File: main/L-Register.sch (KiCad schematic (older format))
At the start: 19 parts, among them U86 74LS245, U87 74LS173, U88 74LS173

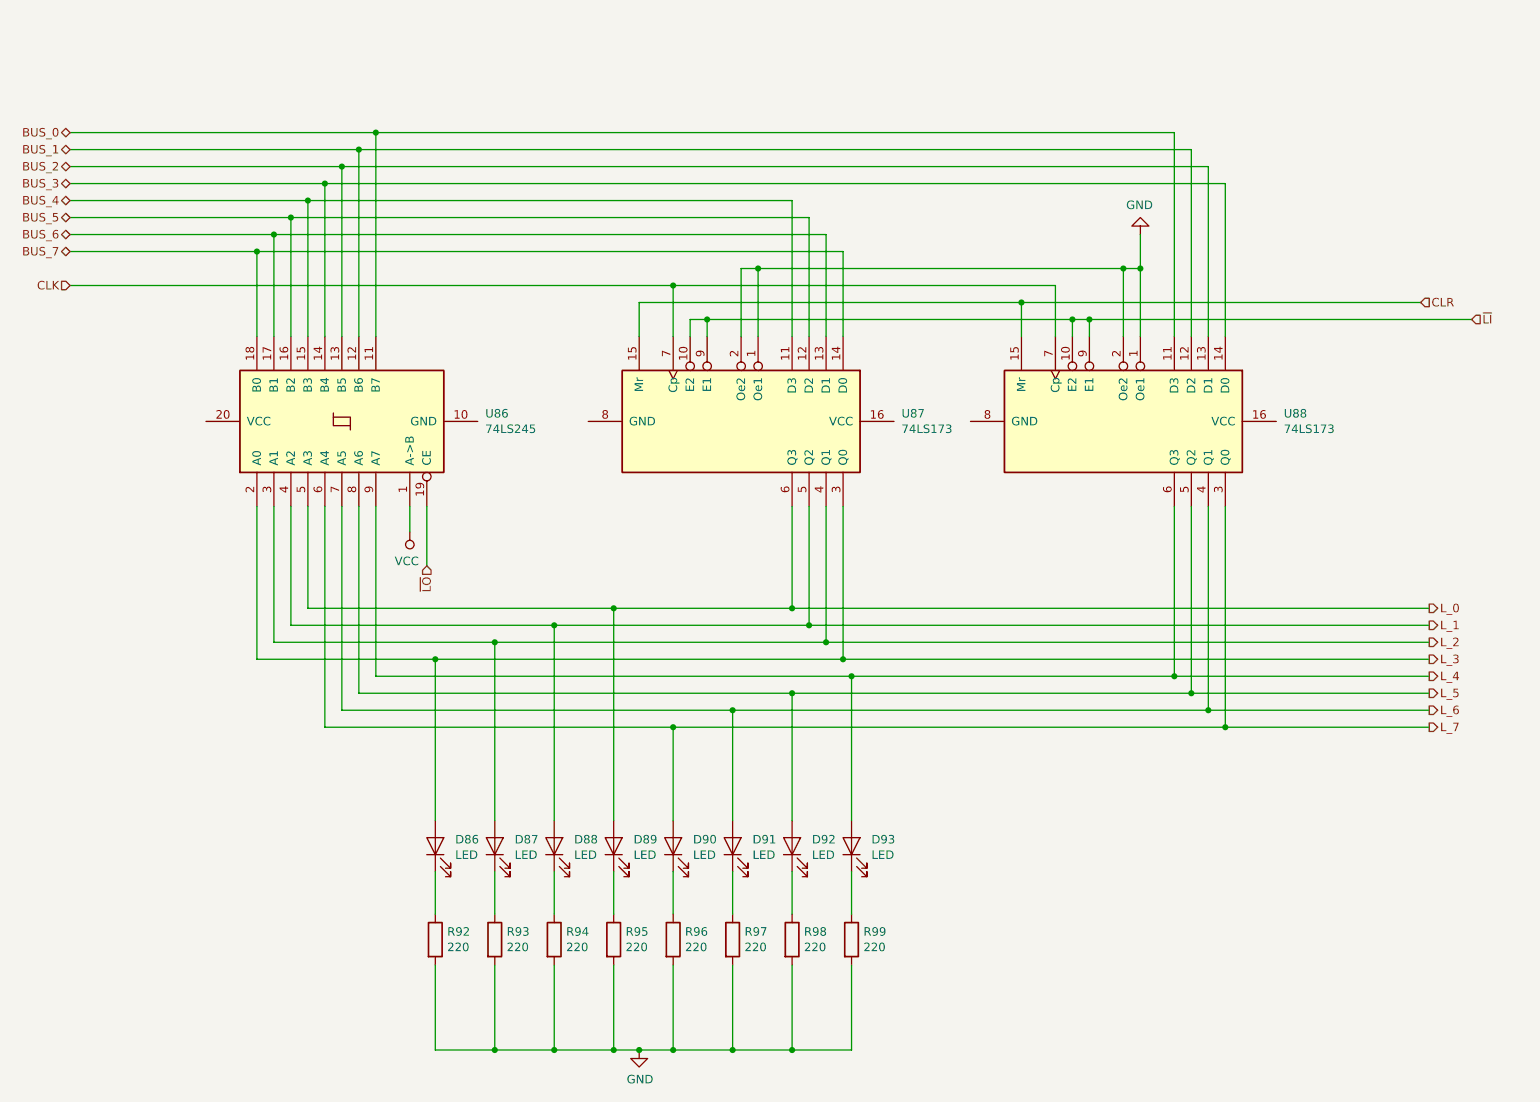
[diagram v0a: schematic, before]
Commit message: Replot main with symbols
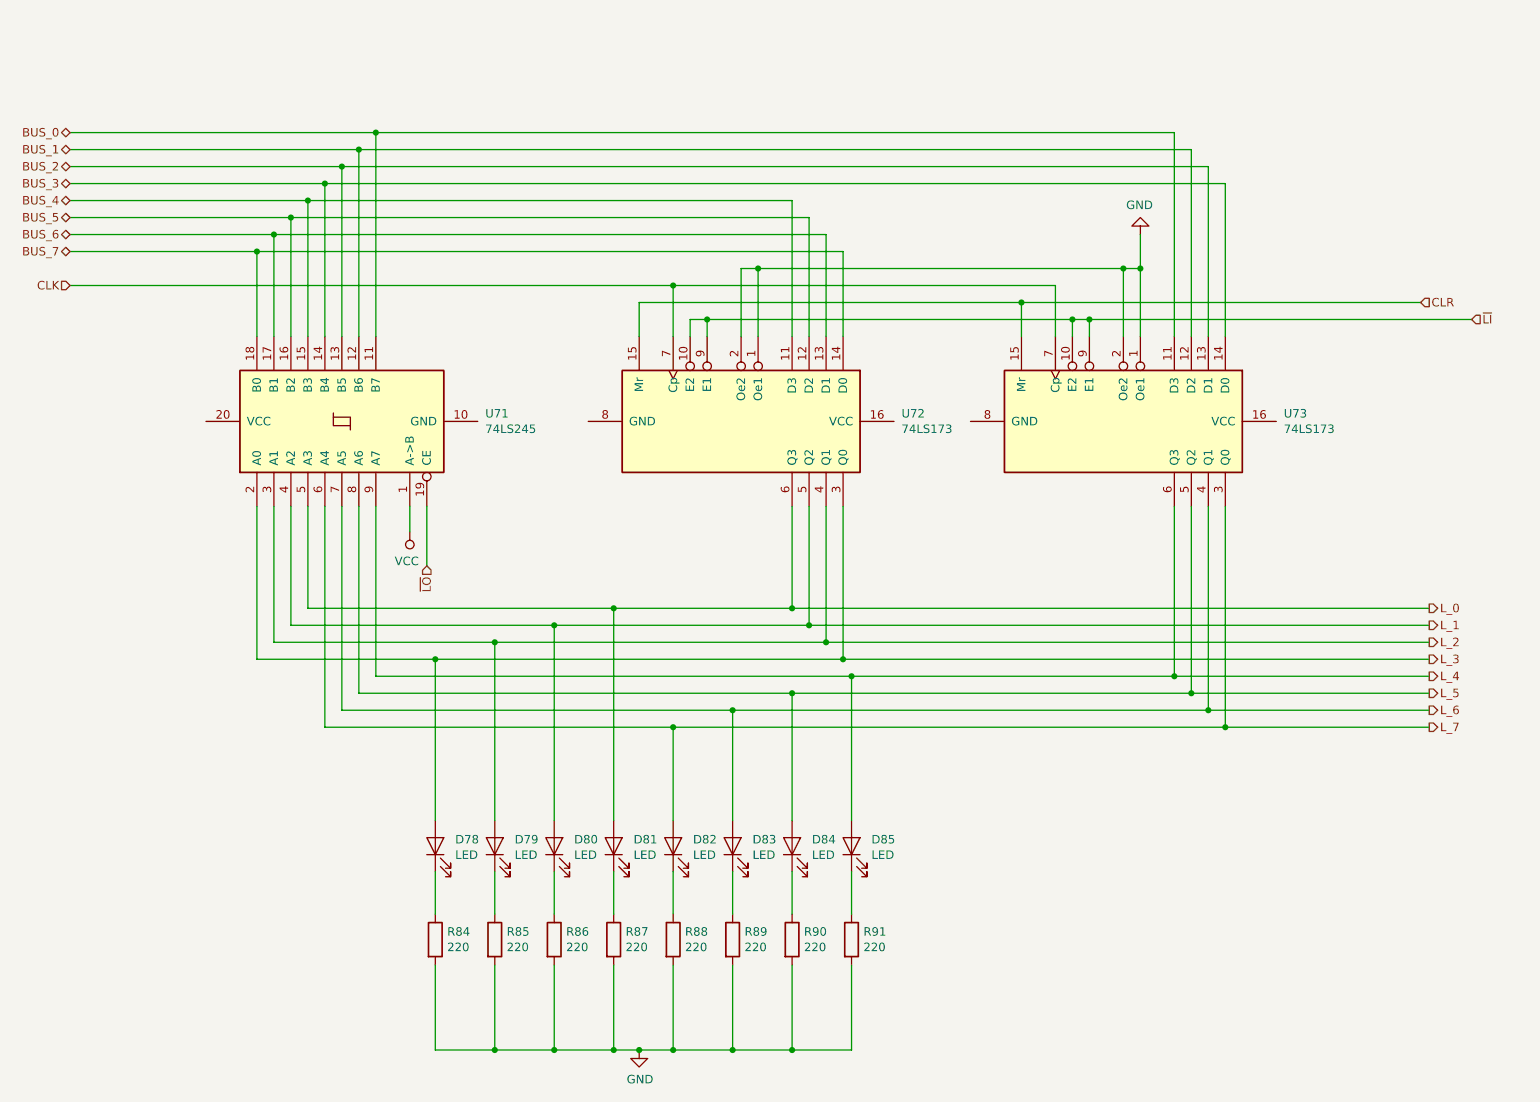
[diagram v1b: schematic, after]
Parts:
- renumbered D86 to D78, D87 to D79, D88 to D80, D89 to D81, D90 to D82, D91 to D83, D92 to D84, D93 to D85, R92 to R84, R93 to R85, R94 to R86, R95 to R87, R96 to R88, R97 to R89, R98 to R90, R99 to R91, U86 to U71, U87 to U72, U88 to U73
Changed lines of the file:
@@
 Sheet 20 26
 Title "L Register"
-Date "2019-11-13"
+Date "2019-11-17"
 Rev "v1.0"
 Comp "Christopher Milan"
@@
 AR Path="/5D9C73BD/5DA803F5" Ref="U?"  Part="1"
 AR Path="/5D9E8F35/5DA803F5" Ref="U?"  Part="1"
-AR Path="/5DA98D6D/5DA9A5C9/5DA803F5" Ref="U86"  Part="1"
-F 0 "U86" V 2896 2456 50  0000 R CNN
+AR Path="/5DA98D6D/5DA9A5C9/5DA803F5" Ref="U71"  Part="1"
+F 0 "U71" V 2896 2456 50  0000 R CNN
 F 1 "74LS245" V 2805 2456 50  0000 R CNN
 F 2 "" H 2850 3300 50  0001 C CNN
@@
 AR Path="/5D9C73BD/5DA80422" Ref="U?"  Part="1"
 AR Path="/5D9E8F35/5DA80422" Ref="U?"  Part="1"
-AR Path="/5DA98D6D/5DA9A5C9/5DA80422" Ref="U88"  Part="1"
-F 0 "U88" V 7404 4244 50  0000 L CNN
+AR Path="/5DA98D6D/5DA9A5C9/5DA80422" Ref="U73"  Part="1"
+F 0 "U73" V 7404 4244 50  0000 L CNN
 F 1 "74LS173" V 7495 4244 50  0000 L CNN
 F 2 "" H 7450 3300 50  0001 C CNN
@@
 AR Path="/5D9C73BD/5DA8044C" Ref="D?"  Part="1"
 AR Path="/5D9E8F35/5DA8044C" Ref="D?"  Part="1"
-AR Path="/5DA98D6D/5DA9A5C9/5DA8044C" Ref="D86"  Part="1"
-F 0 "D86" V 3439 5683 50  0000 R CNN
+AR Path="/5DA98D6D/5DA9A5C9/5DA8044C" Ref="D78"  Part="1"
+F 0 "D78" V 3439 5683 50  0000 R CNN
 F 1 "LED" V 3348 5683 50  0000 R CNN
 F 2 "" H 3400 5800 50  0001 C CNN
@@
 AR Path="/5D9C73BD/5DA80452" Ref="D?"  Part="1"
 AR Path="/5D9E8F35/5DA80452" Ref="D?"  Part="1"
-AR Path="/5DA98D6D/5DA9A5C9/5DA80452" Ref="D87"  Part="1"
-F 0 "D87" V 3789 5683 50  0000 R CNN
+AR Path="/5DA98D6D/5DA9A5C9/5DA80452" Ref="D79"  Part="1"
+F 0 "D79" V 3789 5683 50  0000 R CNN
 F 1 "LED" V 3698 5683 50  0000 R CNN
 F 2 "" H 3750 5800 50  0001 C CNN
@@
 AR Path="/5D9C73BD/5DA80458" Ref="D?"  Part="1"
 AR Path="/5D9E8F35/5DA80458" Ref="D?"  Part="1"
-AR Path="/5DA98D6D/5DA9A5C9/5DA80458" Ref="D88"  Part="1"
-F 0 "D88" V 4139 5683 50  0000 R CNN
+AR Path="/5DA98D6D/5DA9A5C9/5DA80458" Ref="D80"  Part="1"
+F 0 "D80" V 4139 5683 50  0000 R CNN
 F 1 "LED" V 4048 5683 50  0000 R CNN
 F 2 "" H 4100 5800 50  0001 C CNN
@@
 AR Path="/5D9C73BD/5DA8045E" Ref="D?"  Part="1"
 AR Path="/5D9E8F35/5DA8045E" Ref="D?"  Part="1"
-AR Path="/5DA98D6D/5DA9A5C9/5DA8045E" Ref="D89"  Part="1"
-F 0 "D89" V 4489 5683 50  0000 R CNN
+AR Path="/5DA98D6D/5DA9A5C9/5DA8045E" Ref="D81"  Part="1"
+F 0 "D81" V 4489 5683 50  0000 R CNN
 F 1 "LED" V 4398 5683 50  0000 R CNN
 F 2 "" H 4450 5800 50  0001 C CNN
@@
 AR Path="/5D9C73BD/5DA80464" Ref="D?"  Part="1"
 AR Path="/5D9E8F35/5DA80464" Ref="D?"  Part="1"
-AR Path="/5DA98D6D/5DA9A5C9/5DA80464" Ref="D90"  Part="1"
-F 0 "D90" V 4839 5683 50  0000 R CNN
+AR Path="/5DA98D6D/5DA9A5C9/5DA80464" Ref="D82"  Part="1"
+F 0 "D82" V 4839 5683 50  0000 R CNN
 F 1 "LED" V 4748 5683 50  0000 R CNN
 F 2 "" H 4800 5800 50  0001 C CNN
@@
 AR Path="/5D9C73BD/5DA8046A" Ref="D?"  Part="1"
 AR Path="/5D9E8F35/5DA8046A" Ref="D?"  Part="1"
-AR Path="/5DA98D6D/5DA9A5C9/5DA8046A" Ref="D91"  Part="1"
-F 0 "D91" V 5189 5683 50  0000 R CNN
+AR Path="/5DA98D6D/5DA9A5C9/5DA8046A" Ref="D83"  Part="1"
+F 0 "D83" V 5189 5683 50  0000 R CNN
 F 1 "LED" V 5098 5683 50  0000 R CNN
 F 2 "" H 5150 5800 50  0001 C CNN
@@
 AR Path="/5D9C73BD/5DA80470" Ref="D?"  Part="1"
 AR Path="/5D9E8F35/5DA80470" Ref="D?"  Part="1"
-AR Path="/5DA98D6D/5DA9A5C9/5DA80470" Ref="D92"  Part="1"
-F 0 "D92" V 5539 5683 50  0000 R CNN
+AR Path="/5DA98D6D/5DA9A5C9/5DA80470" Ref="D84"  Part="1"
+F 0 "D84" V 5539 5683 50  0000 R CNN
 F 1 "LED" V 5448 5683 50  0000 R CNN
 F 2 "" H 5500 5800 50  0001 C CNN
@@
 AR Path="/5D9C73BD/5DA80476" Ref="D?"  Part="1"
 AR Path="/5D9E8F35/5DA80476" Ref="D?"  Part="1"
-AR Path="/5DA98D6D/5DA9A5C9/5DA80476" Ref="D93"  Part="1"
-F 0 "D93" V 5889 5683 50  0000 R CNN
+AR Path="/5DA98D6D/5DA9A5C9/5DA80476" Ref="D85"  Part="1"
+F 0 "D85" V 5889 5683 50  0000 R CNN
 F 1 "LED" V 5798 5683 50  0000 R CNN
 F 2 "" H 5850 5800 50  0001 C CNN
@@
 AR Path="/5D9C73BD/5DA80492" Ref="R?"  Part="1"
 AR Path="/5D9E8F35/5DA80492" Ref="R?"  Part="1"
-AR Path="/5DA98D6D/5DA9A5C9/5DA80492" Ref="R92"  Part="1"
-F 0 "R92" H 3470 6396 50  0000 L CNN
+AR Path="/5DA98D6D/5DA9A5C9/5DA80492" Ref="R84"  Part="1"
+F 0 "R84" H 3470 6396 50  0000 L CNN
 F 1 "220" H 3470 6305 50  0000 L CNN
 F 2 "" V 3330 6350 50  0001 C CNN
@@
 AR Path="/5D9C73BD/5DA80498" Ref="R?"  Part="1"
 AR Path="/5D9E8F35/5DA80498" Ref="R?"  Part="1"
-AR Path="/5DA98D6D/5DA9A5C9/5DA80498" Ref="R93"  Part="1"
-F 0 "R93" H 3820 6396 50  0000 L CNN
+AR Path="/5DA98D6D/5DA9A5C9/5DA80498" Ref="R85"  Part="1"
+F 0 "R85" H 3820 6396 50  0000 L CNN
 F 1 "220" H 3820 6305 50  0000 L CNN
 F 2 "" V 3680 6350 50  0001 C CNN
@@
 AR Path="/5D9C73BD/5DA8049E" Ref="R?"  Part="1"
 AR Path="/5D9E8F35/5DA8049E" Ref="R?"  Part="1"
-AR Path="/5DA98D6D/5DA9A5C9/5DA8049E" Ref="R94"  Part="1"
-F 0 "R94" H 4170 6396 50  0000 L CNN
+AR Path="/5DA98D6D/5DA9A5C9/5DA8049E" Ref="R86"  Part="1"
+F 0 "R86" H 4170 6396 50  0000 L CNN
 F 1 "220" H 4170 6305 50  0000 L CNN
 F 2 "" V 4030 6350 50  0001 C CNN
@@
 AR Path="/5D9C73BD/5DA804A4" Ref="R?"  Part="1"
 AR Path="/5D9E8F35/5DA804A4" Ref="R?"  Part="1"
-AR Path="/5DA98D6D/5DA9A5C9/5DA804A4" Ref="R95"  Part="1"
-F 0 "R95" H 4520 6396 50  0000 L CNN
+AR Path="/5DA98D6D/5DA9A5C9/5DA804A4" Ref="R87"  Part="1"
+F 0 "R87" H 4520 6396 50  0000 L CNN
 F 1 "220" H 4520 6305 50  0000 L CNN
 F 2 "" V 4380 6350 50  0001 C CNN
@@
 AR Path="/5D9C73BD/5DA804AA" Ref="R?"  Part="1"
 AR Path="/5D9E8F35/5DA804AA" Ref="R?"  Part="1"
-AR Path="/5DA98D6D/5DA9A5C9/5DA804AA" Ref="R96"  Part="1"
-F 0 "R96" H 4870 6396 50  0000 L CNN
+AR Path="/5DA98D6D/5DA9A5C9/5DA804AA" Ref="R88"  Part="1"
+F 0 "R88" H 4870 6396 50  0000 L CNN
 F 1 "220" H 4870 6305 50  0000 L CNN
 F 2 "" V 4730 6350 50  0001 C CNN
@@
 AR Path="/5D9C73BD/5DA804B0" Ref="R?"  Part="1"
 AR Path="/5D9E8F35/5DA804B0" Ref="R?"  Part="1"
-AR Path="/5DA98D6D/5DA9A5C9/5DA804B0" Ref="R97"  Part="1"
-F 0 "R97" H 5220 6396 50  0000 L CNN
+AR Path="/5DA98D6D/5DA9A5C9/5DA804B0" Ref="R89"  Part="1"
+F 0 "R89" H 5220 6396 50  0000 L CNN
 F 1 "220" H 5220 6305 50  0000 L CNN
 F 2 "" V 5080 6350 50  0001 C CNN
@@
 AR Path="/5D9C73BD/5DA804B6" Ref="R?"  Part="1"
 AR Path="/5D9E8F35/5DA804B6" Ref="R?"  Part="1"
-AR Path="/5DA98D6D/5DA9A5C9/5DA804B6" Ref="R98"  Part="1"
-F 0 "R98" H 5570 6396 50  0000 L CNN
+AR Path="/5DA98D6D/5DA9A5C9/5DA804B6" Ref="R90"  Part="1"
+F 0 "R90" H 5570 6396 50  0000 L CNN
 F 1 "220" H 5570 6305 50  0000 L CNN
 F 2 "" V 5430 6350 50  0001 C CNN
@@
 AR Path="/5D9C73BD/5DA804BC" Ref="R?"  Part="1"
 AR Path="/5D9E8F35/5DA804BC" Ref="R?"  Part="1"
-AR Path="/5DA98D6D/5DA9A5C9/5DA804BC" Ref="R99"  Part="1"
-F 0 "R99" H 5920 6396 50  0000 L CNN
+AR Path="/5DA98D6D/5DA9A5C9/5DA804BC" Ref="R91"  Part="1"
+F 0 "R91" H 5920 6396 50  0000 L CNN
 F 1 "220" H 5920 6305 50  0000 L CNN
 F 2 "" V 5780 6350 50  0001 C CNN
@@
 AR Path="/5D9C73BD/5DA8050D" Ref="U?"  Part="1"
 AR Path="/5D9E8F35/5DA8050D" Ref="U?"  Part="1"
-AR Path="/5DA98D6D/5DA9A5C9/5DA8050D" Ref="U87"  Part="1"
-F 0 "U87" V 5154 4244 50  0000 L CNN
+AR Path="/5DA98D6D/5DA9A5C9/5DA8050D" Ref="U72"  Part="1"
+F 0 "U72" V 5154 4244 50  0000 L CNN
 F 1 "74LS173" V 5245 4244 50  0000 L CNN
 F 2 "" H 5200 3300 50  0001 C CNN

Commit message: Switch to using 74LS377 in place of two 74LS173
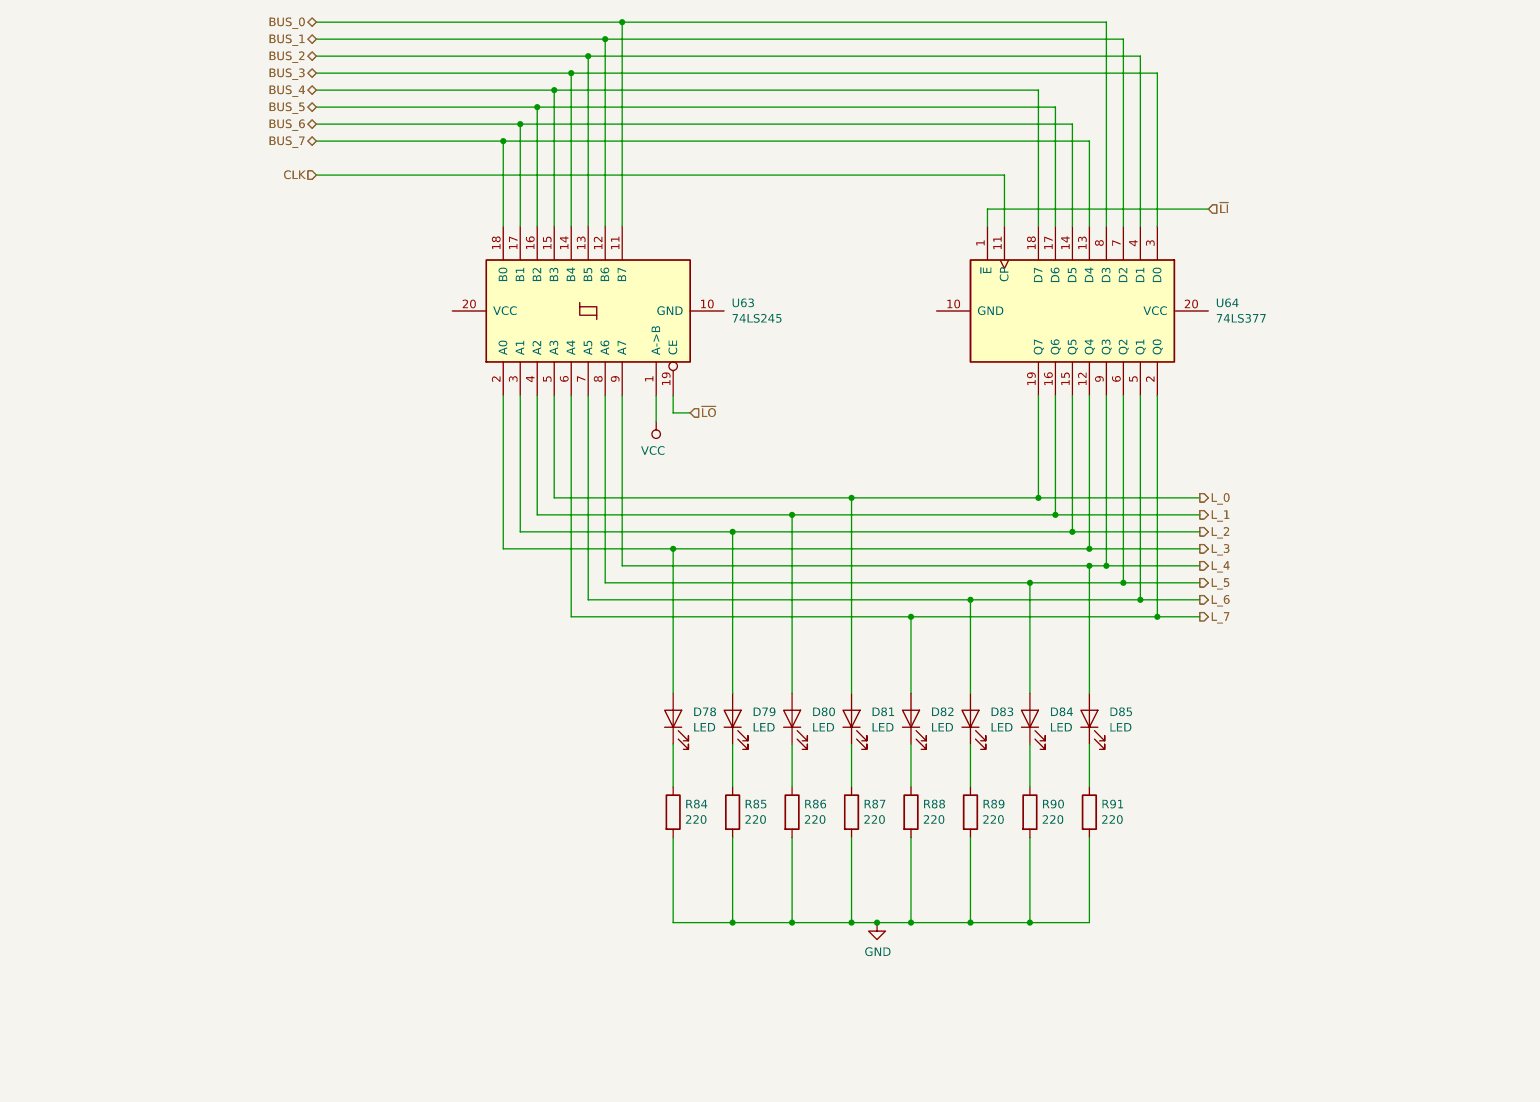
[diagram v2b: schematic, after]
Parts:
- removed U71: 74LS245, symbol 74xx:74LS245
- removed U72, U73: 74LS173, symbol 74xx:74LS173
- added U63: 74LS245, symbol 74xx:74LS245
- added U64: 74LS377, symbol 74xx:74LS377
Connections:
- net BUS_0: now also U63.11 (B7), U64.8 (D3)
- net BUS_1: now also U63.12 (B6), U64.7 (D2)
- net BUS_2: now also U63.13 (B5), U64.4 (D1)
- net BUS_3: now also U63.14 (B4), U64.3 (D0)
- net BUS_4: now also U63.15 (B3), U64.18 (D7)
- net BUS_5: now also U63.16 (B2), U64.17 (D6)
- net BUS_6: now also U63.17 (B1), U64.14 (D5)
- net BUS_7: now also U63.18 (B0), U64.13 (D4)
- net CLK: now also U64.11 (CP)
- net L_0: now also U63.5 (A3), U64.19 (Q7)
- net L_1: now also U63.4 (A2), U64.16 (Q6)
- net L_2: now also U63.3 (A1), U64.15 (Q5)
- net L_3: now also U63.2 (A0), U64.12 (Q4)
- net L_4: now also U63.9 (A7), U64.9 (Q3)
- net L_5: now also U63.8 (A6), U64.6 (Q2)
- net L_6: now also U63.7 (A5), U64.5 (Q1)
- net L_7: now also U63.6 (A4), U64.2 (Q0)
- net VCC: now also U63.1 (A->B)
- net ~LI~: now also U64.1 (~E)
- net ~LO~: now also U63.19 (CE)
